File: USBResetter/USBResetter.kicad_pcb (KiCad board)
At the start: 2 copper layers, 42.6 x 20 mm, 13 parts, among them J1 USB In, J2 USB On, J3 USB Out, Q1 BC547, SW1 Bypass, U1 ASSR-1218

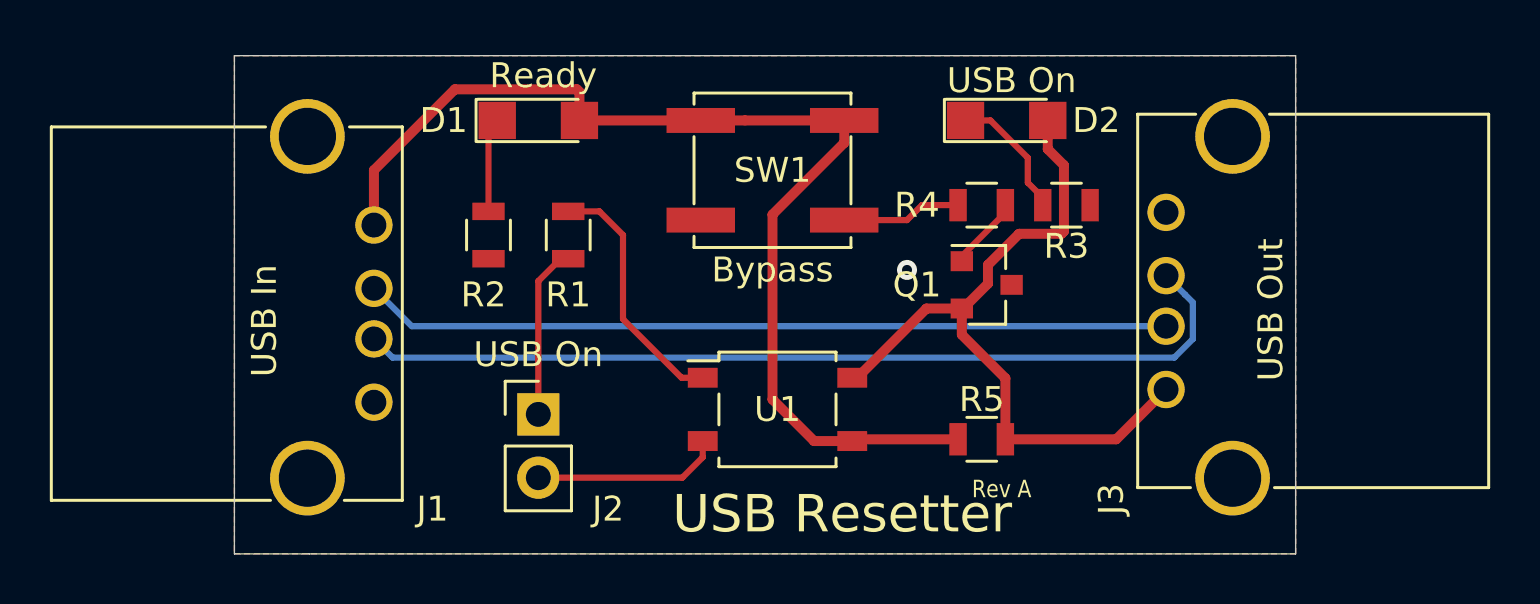
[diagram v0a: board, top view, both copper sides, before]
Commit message: Fixed issues with components and layout
Replaced Footprint for NPN Transistor to match the Pinout of the Part. Recreated the Data lines using Differential Pair to ensure optimal USB Data speed and minimal interference.
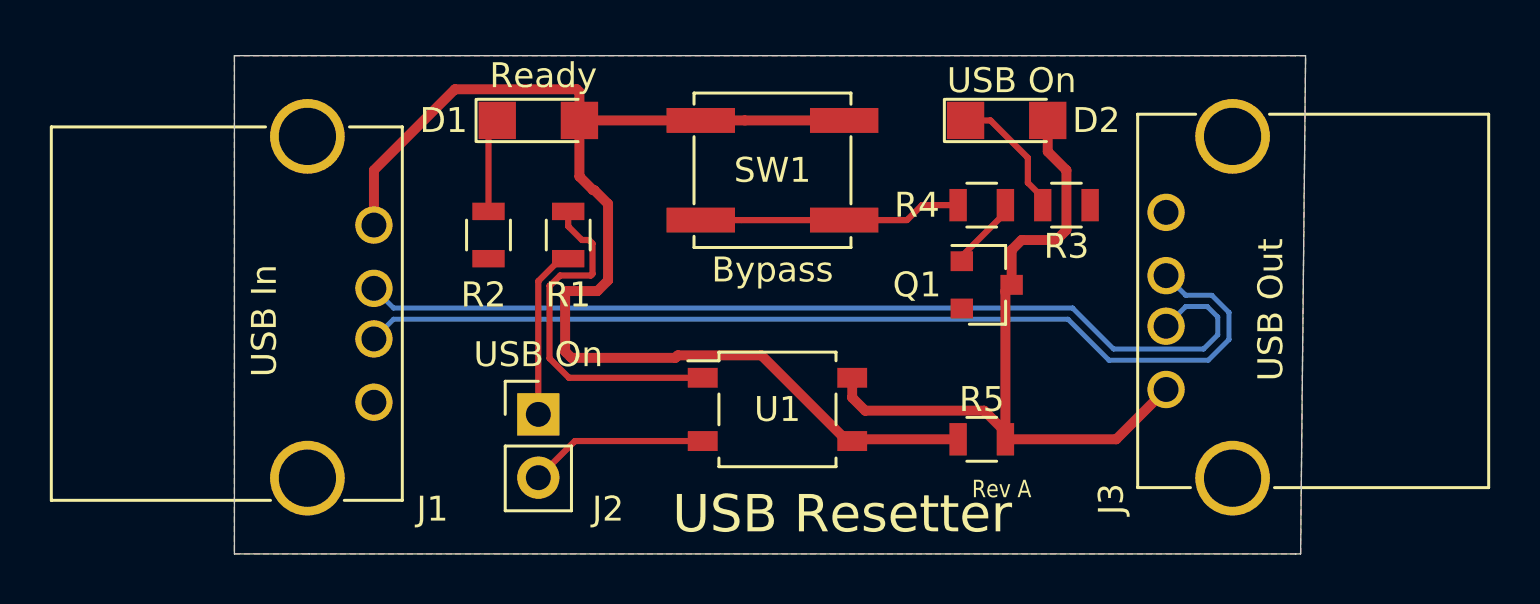
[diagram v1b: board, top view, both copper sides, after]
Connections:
- net Net-(J1-Pad2) renamed /USBD-
- net Net-(J1-Pad3) renamed /USBD+
- Q1 pad 2: Bypass -> GND
- Q1 pad 3: GND -> Bypass
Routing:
- net VBUS: track 44.2 -> 52.2 mm
- net /USBD-: track 32.4 -> 38.4 mm
- net Net-(R4-Pad1): track 4.82 -> 10.6 mm
- net Net-(R1-Pad2): track 10.1 -> 14.4 mm
- net /USBD+: track 36.5 -> 39.9 mm
- net Bypass: track 29.3 -> 30.0 mm
- net GND: vias 1 -> 0
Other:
- board size 42.6 x 20 mm -> 43 x 20 mm
